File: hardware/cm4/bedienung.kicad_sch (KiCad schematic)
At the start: 9 parts, among them SW1 Taste

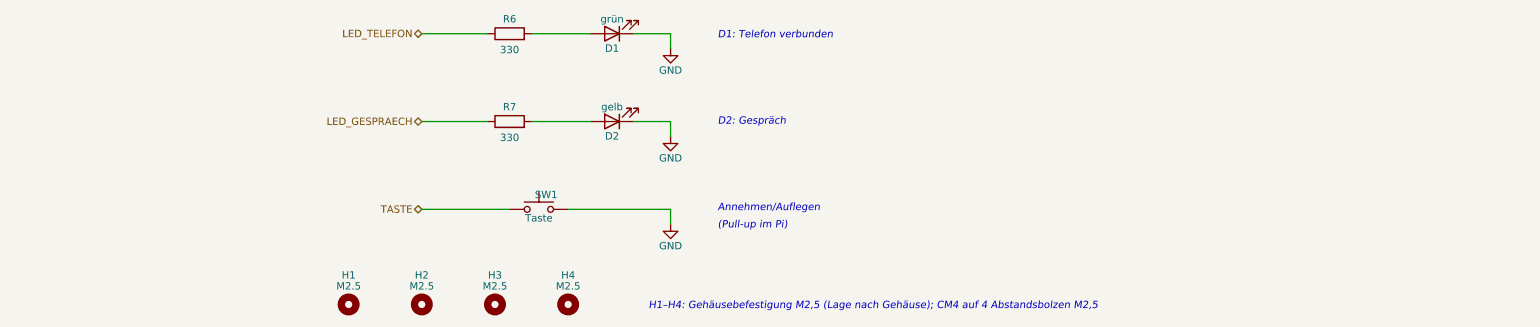
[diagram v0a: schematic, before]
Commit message: CM4-Träger 0.3: Leiterplatte (4 Lagen, JLCPCB), Ein/Aus-Taster, Lüfter, lieferbare Teile
Schaltplan
- Codec TI TLV320AIC3204 statt WM8731 (abgekündigt); MCLK 12 MHz, Reset GPIO26, I²C an GPIO0/1
- Ein/Aus-Taster an GPIO3 (gpio-shutdown im Betrieb, Bootloader-Wecken im Halt)
- Lüfterblatt: AO3400A an GPIO12, Freilaufdiode, JST-PH-Anschluss; gpio-fan über SoC-Temperatur
- Konfig-Taster SW2 und Status-LED D3; Würth RJ45/RJ12, Bourns SM-LP-5001, TPD4E05U06
- reproduzierbare UUIDs (Schaltplan ↔ Platine bleiben verknüpft), eigene Footprints in hardware/bibliothek

Leiterplatte (erzeuge_layout.py)
- 110 × 85 mm, F.Cu / In1 GND / In2 +3V3 / B.Cu, JLC04161H-7628, JLCPCB-Regeln (.kicad_dru)
- CM4-Lage nach CM4IO-Referenz, Antennen-Sperrzone, isolierte Bereiche GND_ISO/GNDA mit Trennstreifen
- eigenes Fanout zu den Ebenen, Routing mit FreeRouting 1.9.0 über xvfb (2.x: Telemetrie an)
- DRC ohne Verstöße, 0 offene Verbindungen, Schaltplan ↔ Platine identisch
- Bestellliste für Digikey mit geprüftem Lagerbestand
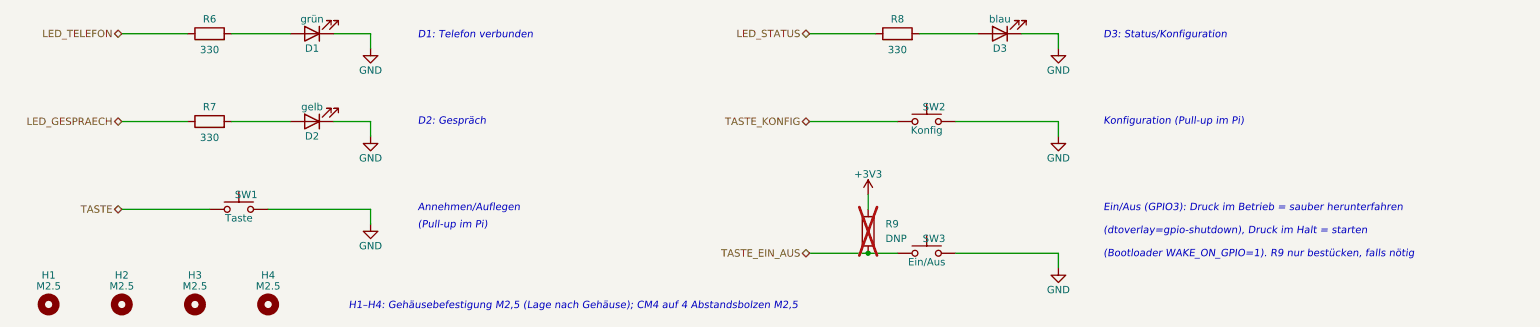
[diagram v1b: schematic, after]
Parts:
- added D3: blau, LED_SMD:LED_0603_1608Metric, symbol Device:LED
- added R8: 330, Resistor_SMD:R_0603_1608Metric, symbol Device:R
- added R9: DNP, Resistor_SMD:R_0603_1608Metric, symbol Device:R
- added SW2: Konfig, Button_Switch_SMD:SW_SPST_TL3342, symbol Switch:SW_Push
- added SW3: Ein/Aus, Button_Switch_SMD:SW_SPST_TL3342, symbol Switch:SW_Push
- H1, H2, H3, H4: now left out of the parts list
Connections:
- net GND: now also D3.1 (K), SW2.2, SW3.2
- new net: D3.2 (A), R8.2
- new net +3V3: R9.1
- new net LED_STATUS: R8.1
- new net TASTE_EIN_AUS: R9.2, SW3.1
- new net TASTE_KONFIG: SW2.1
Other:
- note added: "(Bootloader WAKE_ON_GPIO=1). R9 nur bestücken, falls nötig"
- note added: "(dtoverlay=gpio-shutdown), Druck im Halt = starten"
- note added: "D3: Status/Konfiguration"
- note added: "Ein/Aus (GPIO3): Druck im Betrieb = sauber herunterfahren"
- note added: "Konfiguration (Pull-up im Pi)"

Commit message: Schaltplan: Hinweise als Textkästen (KiCad bricht um); Texte werden in den Generator zurückgeführt
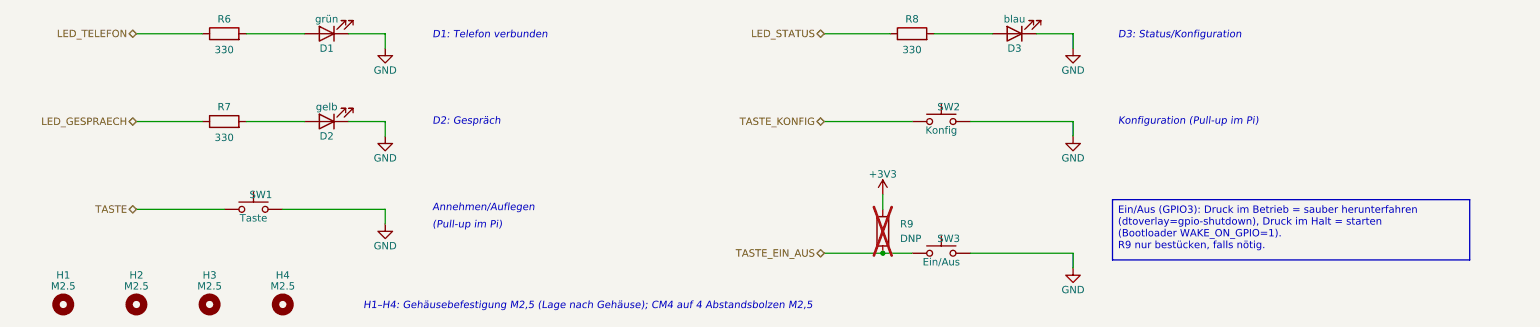
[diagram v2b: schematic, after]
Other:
- note removed: "(Bootloader WAKE_ON_GPIO=1). R9 nur bestücken, falls nötig"
- note removed: "(dtoverlay=gpio-shutdown), Druck im Halt = starten"
- note removed: "Ein/Aus (GPIO3): Druck im Betrieb = sauber herunterfahren"
- moved on the sheet: D1, D2, D3, H1, H2, H3, H4, R6, R7, R8, R9, SW1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
